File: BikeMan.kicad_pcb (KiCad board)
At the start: 2 copper layers, 65 parts, among them J1 USB_A_stacked, J2 USB_A_stacked, J6 MagJack, Q1 AUIRF7316QTR, Q2 AUIRF7316QTR, Q3 AUIRF7316QTR, Q4 AUIRF7316QTR, U1 MCP2515, U2 MCP2551, U4 RT9742GGJ5, U5 NPIC6C596ADJ, U8 TUSB2046IBVF

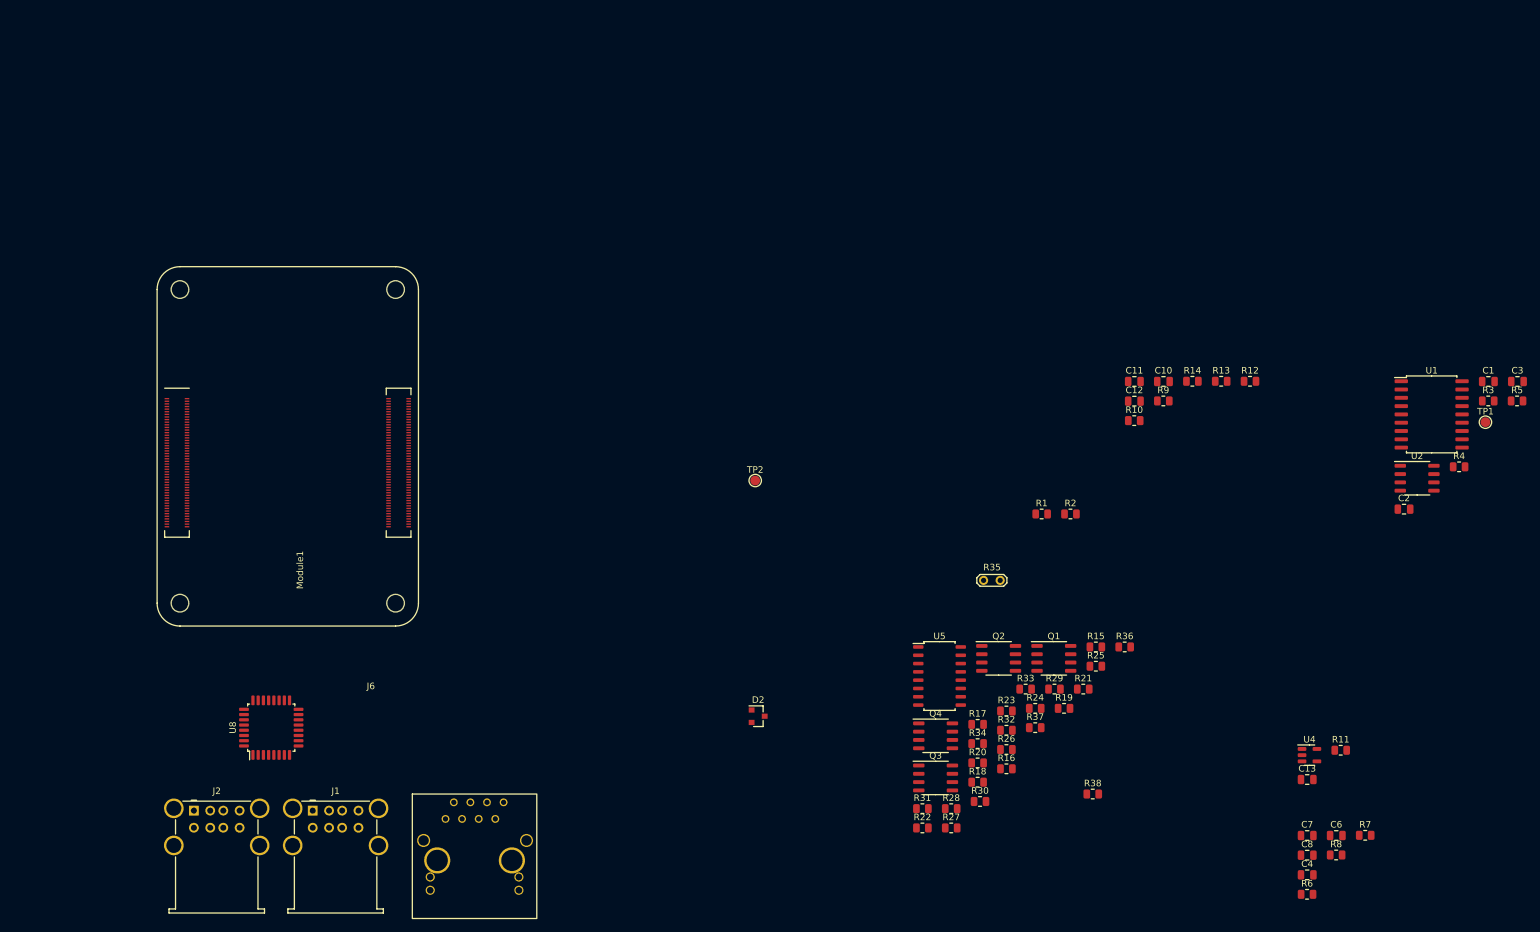
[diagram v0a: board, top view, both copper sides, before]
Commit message: Adding footprints and step files for connectors
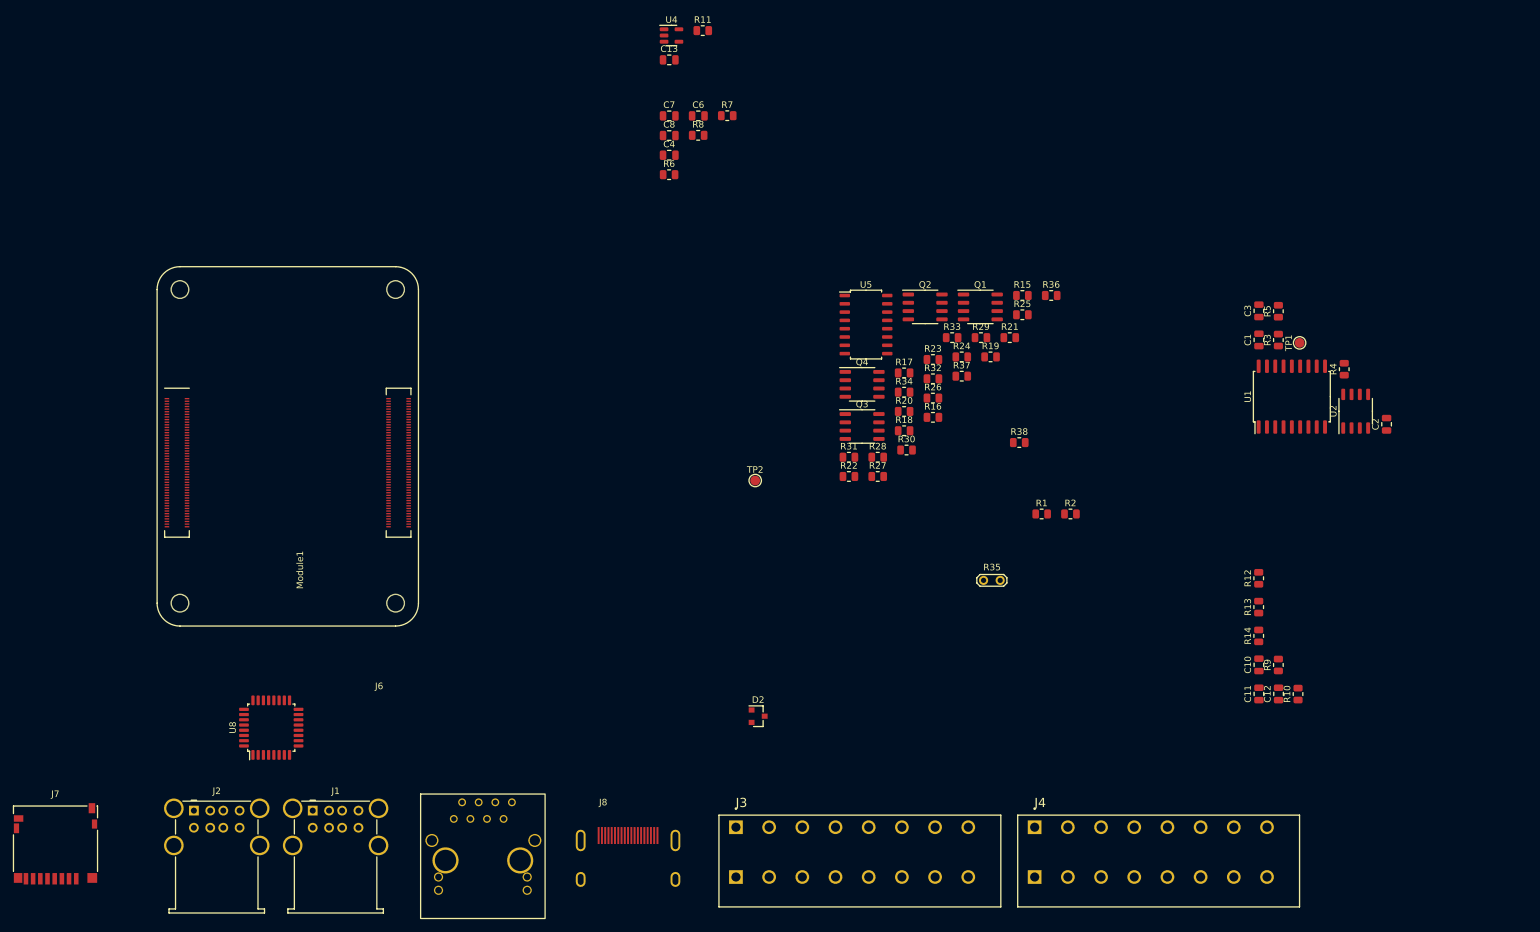
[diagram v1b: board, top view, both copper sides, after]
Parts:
- added J3: PushConnector_8pos, footprints:CUI_TBL004-508-08BE-2BE, F.Cu at (129.5, 125.7)
- added J4: PushConnector_8pos, footprints:CUI_TBL004-508-08BE-2BE, F.Cu at (175.3, 125.7)
- added J7: Micro_SD_Card_Det, Connector_Card:microSD_HC_Hirose_DM3D-SF, F.Cu at (25.4, 128.3)
- added J8: HDMI_A_1.4, footprints:HDMI_Molex-2086588131, F.Cu at (113.0, 127.0)
- moved C13 147.2 mm to (119.3, 8.29)
- moved C4 147.2 mm to (119.3, 22.9)
- moved C6 147.2 mm to (123.8, 16.9)
- moved C7 147.2 mm to (119.3, 16.9)
- moved C8 147.2 mm to (119.3, 19.9)
- moved R11 147.2 mm to (124.5, 3.81)
- moved R6 147.2 mm to (119.3, 25.9)
- moved R7 147.2 mm to (128.2, 16.8)
- moved R8 147.2 mm to (123.8, 19.8)
- moved U4 147.2 mm to (119.7, 4.56)
- moved R16 55.0 mm to (159.7, 63.0)
- moved R18 55.0 mm to (155.3, 65.0)
- moved R19 55.0 mm to (168.5, 53.8)
- moved R21 55.0 mm to (171.4, 50.8)
- moved R24 55.0 mm to (164.1, 53.8)
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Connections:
- J2 pad 1: /D_{4}+ -> +5V
- J2 pad 2: Net-(J2-Pad2) -> /D_{4}+

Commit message: WIP
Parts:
- moved D2 36.5 mm to (163.8, 128.3)
- moved Q3 36.5 mm to (179.7, 83.9)
- moved Q4 36.5 mm to (179.7, 77.5)
- moved R10 36.5 mm to (246.5, 124.9)
- moved R15 36.5 mm to (204.3, 63.9)
- moved R16 36.5 mm to (190.6, 82.5)
- moved R19 36.5 mm to (199.4, 73.3)
- moved R21 36.5 mm to (202.3, 70.3)
- moved R23 36.5 mm to (190.6, 73.7)
- moved R24 36.5 mm to (195.0, 73.3)
- moved R25 36.5 mm to (204.3, 66.8)
- moved R26 36.5 mm to (190.6, 79.6)
- moved R29 36.5 mm to (197.9, 70.3)
- moved R33 36.5 mm to (193.5, 70.3)
- moved R35 36.5 mm to (198.3, 107.5)
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
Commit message: footprint assignments
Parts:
- added BT1: Battery_Cell, Battery:BatteryHolder_Keystone_3001_1x12mm, F.Cu at (113.0, 106.3)
- added J4: Barrel_Jack, Connector_BarrelJack:BarrelJack_Horizontal, F.Cu at (132.1, 141.0)
- added J7: PushConnector_8pos, footprints:CUI_TBL004-508-08BE-2BE, F.Cu at (57.6, 28.4)
- added JP1: SolderJumper_2_Open, Jumper:SolderJumper-2_P1.3mm_Open_RoundedPad1.0x1.5mm, F.Cu at (174.5, 65.3)
- added JP3: SolderJumper_2_Open, Jumper:SolderJumper-2_P1.3mm_Open_RoundedPad1.0x1.5mm, F.Cu at (174.5, 68.9)
- added JP4: SolderJumper_2_Open, Jumper:SolderJumper-2_P1.3mm_Open_RoundedPad1.0x1.5mm, F.Cu at (247.7, 62.2)
- added U3: AP64501, Package_SO:SOIC-8-1EP_3.9x4.9mm_P1.27mm_EP2.514x3.2mm, F.Cu at (249.7, 57.2)
- added U6: PCF8574DWR, Package_SO:SOIC-16W_7.5x10.3mm_P1.27mm, F.Cu at (225.5, 51.0)
- added U7: PCF85063A, Package_SO:SOIC-8_3.9x4.9mm_P1.27mm, F.Cu at (194.9, 48.3)
- moved J6 156.3 mm to (102.9, 27.9), turned to 180 degrees
- moved U4 125.3 mm to (152.1, 149.3)
- moved R11 123.7 mm to (162.3, 146.8)
- moved J5 117.9 mm to (148.6, 27.9), turned to 180 degrees
- moved C13 112.7 mm to (153.4, 140.4)
- moved C4 96.1 mm to (168.9, 136.7)
- moved C8 96.1 mm to (168.9, 133.7)
- moved R8 96.1 mm to (173.4, 133.7)
- moved C6 96.1 mm to (173.4, 130.7)
- moved C7 96.1 mm to (168.9, 130.7)
- moved R6 96.1 mm to (168.9, 139.7)
- moved R7 96.1 mm to (177.8, 130.7)
- moved Q2 78.1 mm to (115.6, 40.0), turned to 90 degrees
- moved Q1 77.8 mm to (124.4, 40.0), turned to 90 degrees
- moved Q4 59.6 mm to (133.3, 40.0), turned to 90 degrees
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- renumbered D2 to D3, J8 to J10, J3 to J5, J4 to J6, J6 to J8, J7 to J9
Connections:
- net /CAN_{L} renamed /CAN_{L}_1
- J8 pad 1: no_connect_194 -> no_connect_208
- J8 pad 8: no_connect_196 -> no_connect_210
- Module1 pad 10: no_connect_197 -> no_connect_211
- Module1 pad 102: no_connect_198 -> no_connect_212
- Module1 pad 104: no_connect_199 -> no_connect_213
- Module1 pad 106: no_connect_200 -> no_connect_214
- Module1 pad 109: no_connect_201 -> no_connect_215
- Module1 pad 110: no_connect_202 -> no_connect_216
- Module1 pad 111: no_connect_203 -> no_connect_217
- Module1 pad 112: no_connect_204 -> no_connect_218
- Module1 pad 115: no_connect_205 -> no_connect_219
- Module1 pad 116: no_connect_206 -> no_connect_220
- Module1 pad 117: no_connect_207 -> no_connect_221
- Module1 pad 118: no_connect_208 -> no_connect_222
- Module1 pad 12: no_connect_209 -> no_connect_223
- Module1 pad 121: no_connect_210 -> no_connect_224
- Module1 pad 122: no_connect_211 -> no_connect_225
- Module1 pad 123: no_connect_212 -> no_connect_226
- Module1 pad 124: no_connect_213 -> no_connect_227
- Module1 pad 127: no_connect_214 -> no_connect_228
- Module1 pad 128: no_connect_215 -> no_connect_229
- Module1 pad 129: no_connect_216 -> no_connect_230
- Module1 pad 130: no_connect_217 -> no_connect_231
- Module1 pad 133: no_connect_218 -> no_connect_232
- Module1 pad 134: no_connect_219 -> no_connect_233
- Module1 pad 135: no_connect_220 -> no_connect_234
- Module1 pad 136: no_connect_221 -> no_connect_235
- Module1 pad 139: no_connect_222 -> no_connect_236
- Module1 pad 140: no_connect_223 -> no_connect_237
- Module1 pad 141: no_connect_224 -> no_connect_238
- Module1 pad 142: no_connect_225 -> no_connect_239
- Module1 pad 143: no_connect_226 -> no_connect_240
- Module1 pad 145: no_connect_227 -> no_connect_241
- Module1 pad 146: no_connect_228 -> no_connect_242
- Module1 pad 147: no_connect_229 -> no_connect_243
- Module1 pad 148: no_connect_230 -> no_connect_244
- Module1 pad 149: no_connect_231 -> no_connect_245
- Module1 pad 152: no_connect_232 -> no_connect_246
- Module1 pad 154: no_connect_233 -> no_connect_247
- Module1 pad 157: no_connect_234 -> no_connect_248
- Module1 pad 158: no_connect_235 -> no_connect_249
- Module1 pad 159: no_connect_236 -> no_connect_250
- Module1 pad 160: no_connect_237 -> no_connect_251
- Module1 pad 163: no_connect_238 -> no_connect_252
- Module1 pad 164: no_connect_239 -> no_connect_253
- Module1 pad 165: no_connect_240 -> no_connect_254
- Module1 pad 166: no_connect_241 -> no_connect_255
- Module1 pad 169: no_connect_242 -> no_connect_256
- Module1 pad 171: no_connect_243 -> no_connect_257
- Module1 pad 175: no_connect_244 -> no_connect_258
- Module1 pad 177: no_connect_245 -> no_connect_259
- Module1 pad 181: no_connect_246 -> no_connect_260
- Module1 pad 183: no_connect_247 -> no_connect_261
- Module1 pad 187: no_connect_248 -> no_connect_262
- Module1 pad 189: no_connect_249 -> no_connect_263
- Module1 pad 19: no_connect_250 -> no_connect_264
- Module1 pad 193: no_connect_251 -> no_connect_265
- Module1 pad 195: no_connect_252 -> no_connect_266
- Module1 pad 3: no_connect_253 -> no_connect_267
- Module1 pad 5: no_connect_254 -> no_connect_268
- U1 pad 10: no_connect_255 -> no_connect_269
- U1 pad 11: no_connect_256 -> no_connect_270
- U1 pad 3: no_connect_257 -> no_connect_271
- U1 pad 4: no_connect_258 -> no_connect_272
- U1 pad 5: no_connect_259 -> no_connect_273
- U1 pad 6: no_connect_260 -> no_connect_274
- U2 pad 5: no_connect_261 -> no_connect_275
- U2 pad 7: /CAN_{H} -> /CAN_{H}_1
- U5 pad 9: no_connect_262 -> no_connect_276

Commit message: WIP 5 FEB 2021
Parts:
- R35: footprint TestPoint:TestPoint_2Pads_Pitch2.54mm_Drill0.8mm -> Resistor_SMD:R_0805_2012Metric
- moved J4 218.1 mm to (328.9, 47.0)
- moved JP1 165.1 mm to (322.6, 138.4)
- moved U6 144.5 mm to (81.3, 41.9), turned to 90 degrees
- moved R5 135.8 mm to (327.7, 137.2), turned to 180 degrees
- moved BT1 112.7 mm to (209.6, 48.3)
- moved U2 110.3 mm to (322.6, 130.8), turned to 180 degrees
- moved U1 108.3 mm to (308.6, 132.1), turned to 180 degrees
- moved U3 92.4 mm to (340.4, 39.4)
- moved R25 85.0 mm to (92.7, 39.4)
- moved R29 82.2 mm to (92.7, 34.3)
- moved R15 81.6 mm to (92.7, 52.1)
- moved R19 81.4 mm to (96.5, 34.3)
- moved R21 80.4 mm to (96.9, 39.4)
- moved R16 76.5 mm to (92.7, 44.5)
- moved R26 76.3 mm to (92.7, 41.9)
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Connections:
- net Net-(U6-Pad13) renamed /~INT_{GPIO}
- J8 pad 1: no_connect_208 -> no_connect_196
- J8 pad 8: no_connect_210 -> no_connect_198
- Module1 pad 10: no_connect_211 -> no_connect_199
- Module1 pad 102: no_connect_212 -> no_connect_200
- Module1 pad 104: no_connect_213 -> no_connect_201
- Module1 pad 106: no_connect_214 -> no_connect_202
- Module1 pad 109: no_connect_215 -> no_connect_203
- Module1 pad 110: no_connect_216 -> no_connect_204
- Module1 pad 111: no_connect_217 -> no_connect_205
- Module1 pad 112: no_connect_218 -> no_connect_206
- Module1 pad 115: no_connect_219 -> no_connect_207
- Module1 pad 116: no_connect_220 -> no_connect_208
- Module1 pad 117: no_connect_221 -> no_connect_209
- Module1 pad 118: no_connect_222 -> no_connect_210
- Module1 pad 12: no_connect_223 -> no_connect_211
- Module1 pad 121: no_connect_224 -> no_connect_212
- Module1 pad 122: no_connect_225 -> no_connect_213
- Module1 pad 123: no_connect_226 -> no_connect_214
- Module1 pad 124: no_connect_227 -> no_connect_215
- Module1 pad 127: no_connect_228 -> no_connect_216
- Module1 pad 128: no_connect_229 -> no_connect_217
- Module1 pad 129: no_connect_230 -> no_connect_218
- Module1 pad 130: no_connect_231 -> no_connect_219
- Module1 pad 133: no_connect_232 -> no_connect_220
- Module1 pad 134: no_connect_233 -> no_connect_221
- Module1 pad 135: no_connect_234 -> no_connect_222
- Module1 pad 136: no_connect_235 -> no_connect_223
- Module1 pad 139: no_connect_236 -> no_connect_224
- Module1 pad 140: no_connect_237 -> no_connect_225
- Module1 pad 141: no_connect_238 -> no_connect_226
- Module1 pad 142: no_connect_239 -> no_connect_227
- Module1 pad 143: no_connect_240 -> no_connect_228
- Module1 pad 145: no_connect_241 -> no_connect_229
- Module1 pad 146: no_connect_242 -> no_connect_230
- Module1 pad 147: no_connect_243 -> no_connect_231
- Module1 pad 148: no_connect_244 -> no_connect_232
- Module1 pad 149: no_connect_245 -> no_connect_233
- Module1 pad 152: no_connect_246 -> no_connect_234
- Module1 pad 154: no_connect_247 -> no_connect_235
- Module1 pad 157: no_connect_248 -> no_connect_236
- Module1 pad 158: no_connect_249 -> no_connect_237
- Module1 pad 159: no_connect_250 -> no_connect_238
- Module1 pad 160: no_connect_251 -> no_connect_239
- Module1 pad 163: no_connect_252 -> no_connect_240
- Module1 pad 164: no_connect_253 -> no_connect_241
- Module1 pad 165: no_connect_254 -> no_connect_242
- Module1 pad 166: no_connect_255 -> no_connect_243
- Module1 pad 169: no_connect_256 -> no_connect_244
- Module1 pad 171: no_connect_257 -> no_connect_245
- Module1 pad 175: no_connect_258 -> no_connect_246
- Module1 pad 177: no_connect_259 -> no_connect_247
- Module1 pad 181: no_connect_260 -> no_connect_248
- Module1 pad 183: no_connect_261 -> no_connect_249
- Module1 pad 187: no_connect_262 -> no_connect_250
- Module1 pad 189: no_connect_263 -> no_connect_251
- Module1 pad 19: no_connect_264 -> no_connect_252
- Module1 pad 193: no_connect_265 -> no_connect_253
- Module1 pad 195: no_connect_266 -> no_connect_254
- Module1 pad 3: no_connect_267 -> no_connect_255
- Module1 pad 5: no_connect_268 -> no_connect_256
- U1 pad 10: no_connect_269 -> no_connect_257
- U1 pad 11: no_connect_270 -> no_connect_258
- U1 pad 3: no_connect_271 -> no_connect_259
- U1 pad 4: no_connect_272 -> no_connect_260
- U1 pad 5: no_connect_273 -> no_connect_261
- U1 pad 6: no_connect_274 -> no_connect_262
- U2 pad 5: no_connect_275 -> no_connect_263
- U5 pad 9: no_connect_276 -> no_connect_264
- U6 pad 1: Net-(U6-Pad1) -> GND
- U6 pad 10: Net-(U6-Pad10) -> /GPIO/I_{7}
- U6 pad 11: Net-(U6-Pad11) -> /GPIO/I_{6}
- U6 pad 12: Net-(U6-Pad12) -> /GPIO/I_{5}
- U6 pad 14: Net-(U6-Pad14) -> /SCL
- U6 pad 15: Net-(U6-Pad15) -> /SDA
- U6 pad 16: Net-(U6-Pad16) -> +3V3
- U6 pad 2: Net-(U6-Pad1) -> GND
- U6 pad 3: Net-(U6-Pad1) -> GND
- U6 pad 4: Net-(U6-Pad4) -> /GPIO/I_{1}
- U6 pad 5: Net-(U6-Pad5) -> /GPIO/I_{2}
- U6 pad 6: Net-(U6-Pad6) -> /GPIO/I_{3}
- U6 pad 7: GND -> /GPIO/I_{4}
- U6 pad 9: Net-(U6-Pad9) -> /GPIO/I_{8}

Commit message: switched to networked resistors on GPIO system
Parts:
- moved D3 218.7 mm to (346.7, 78.7)
- moved C8 201.8 mm to (348.0, 40.6)
- moved C7 193.7 mm to (344.2, 48.3)
- moved BT1 155.6 mm to (359.4, 90.2)
- moved U7 155.6 mm to (344.8, 90.2)
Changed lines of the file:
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@@
   )
   (footprint "Package_TO_SOT_SMD:SOT-23" (layer "F.Cu")
-    (at 133.27 126.58)
+    (at 346.71 78.74)
     (descr "SOT-23, Standard")
     (tags "SOT-23")
@@
   )
   (footprint "Capacitor_SMD:C_0805_2012Metric" (layer "F.Cu")
-    (at 168.93 133.71)
+    (at 347.98 40.64)
     (descr "Capacitor SMD 0805 (2012 Metric), square (rectangular) end terminal, IPC_7351 nominal, (Body size source: IPC-SM-782 page 76, https://www.pcb-3d.com/wordpress/wp-content/uploads/ipc-sm-782a_amendment_1_and_2.pdf, https://docs.google.com/spreadsheets/d/1BsfQQcO9C6DZCsRaXUlFlo91Tg2WpOkGARC1WS5S8t0/edit?usp=sharing), generated with kicad-footprint-generator")
     (tags "capacitor")
@@
   )
   (footprint "Capacitor_SMD:C_0805_2012Metric" (layer "F.Cu")
-    (at 168.93 130.7)
+    (at 344.17 48.26)
     (descr "Capacitor SMD 0805 (2012 Metric), square (rectangular) end terminal, IPC_7351 nominal, (Body size source: IPC-SM-782 page 76, https://www.pcb-3d.com/wordpress/wp-content/uploads/ipc-sm-782a_amendment_1_and_2.pdf, https://docs.google.com/spreadsheets/d/1BsfQQcO9C6DZCsRaXUlFlo91Tg2WpOkGARC1WS5S8t0/edit?usp=sharing), generated with kicad-footprint-generator")
     (tags "capacitor")
@@
   )
   (footprint "Package_SO:SOIC-8_3.9x4.9mm_P1.27mm" (layer "F.Cu")
-    (at 194.93452 48.27)
+    (at 344.79452 90.18)
     (descr "SOIC, 8 Pin (JEDEC MS-012AA, https://www.analog.com/media/en/package-pcb-resources/package/pkg_pdf/soic_narrow-r/r_8.pdf), generated with kicad-footprint-generator ipc_gullwing_generator.py")
     (tags "SOIC SO")
@@
   )
   (footprint "Battery:BatteryHolder_Keystone_3001_1x12mm" (layer "F.Cu")
-    (at 209.55 48.26)
+    (at 359.41 90.17)
     (descr "http://www.keyelco.com/product-pdf.cfm?p=778")
     (tags "Keystone type 3001 coin cell retainer")
